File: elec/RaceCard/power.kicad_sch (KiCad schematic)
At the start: 12 parts, among them J1 530480210, Q1 DMP3125L-7, U1 TLV74033PDQNR, U2 MCP73812T-420I_OT, U3 AS11AH

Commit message: Choses manquantes
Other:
- note added: "GÉRER LE POWER OUT"
- note added: "METTRE CONN."
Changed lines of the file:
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@@
+		)
+	)
+	(text "METTRE CONN."
+		(exclude_from_sim no)
+		(at 60.706 85.852 0)
+		(effects
+			(font
+				(size 1.27 1.27)
+				(thickness 0.254)
+				(bold yes)
+				(color 255 0 0 1)
+			)
+		)
+	)
+	(text "GÉRER LE POWER OUT"
+		(exclude_from_sim no)
+		(at 230.124 97.282 0)
+		(effects
+			(font
+				(size 1.27 1.27)
+				(thickness 0.254)
+				(bold yes)
+				(color 255 0 0 1)
+			)
 		)
 	)

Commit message: Commence plugger choses
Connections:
- net VDD: now reaches C2.1, D1.2 (A), U1.1 (OUT)
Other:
- note removed: "GÉRER LE POWER OUT"
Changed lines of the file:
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@@
-		)
-	)
-	(text "GÉRER LE POWER OUT"
-		(exclude_from_sim no)
-		(at 230.124 97.282 0)
-		(effects
-			(font
-				(size 1.27 1.27)
-				(thickness 0.254)
-				(bold yes)
-				(color 255 0 0 1)
-			)
 		)
 	)
@@
 		(color 0 0 0 0)
 	)
+	(junction
+		(at 218.44 97.79)
+		(diameter 0)
+		(color 0 0 0 0)
+	)
 	(wire
 		(pts
@@
 	(wire
 		(pts
+			(xy 218.44 97.79) (xy 222.25 97.79)
+		)
+		(stroke
+			(width 0)
+			(type default)
+		)
+	)
+	(wire
+		(pts
 			(xy 209.55 104.14) (xy 209.55 105.41)
 		)
@@
 	(wire
 		(pts
+			(xy 218.44 97.79) (xy 218.44 99.06)
+		)
+		(stroke
+			(width 0)
+			(type default)
+		)
+	)
+	(wire
+		(pts
 			(xy 191.77 104.14) (xy 190.5 104.14)
 		)
@@
 		(pts
 			(xy 218.44 104.14) (xy 218.44 105.41)
-		)
-		(stroke
-			(width 0)
-			(type default)
-		)
-	)
-	(wire
-		(pts
-			(xy 218.44 97.79) (xy 218.44 99.06)
 		)
 		(stroke
@@
 		)
 	)
+	(hierarchical_label "VDD"
+		(shape output)
+		(at 222.25 97.79 0)
+		(effects
+			(font
+				(size 1.27 1.27)
+			)
+			(justify left)
+		)
+	)

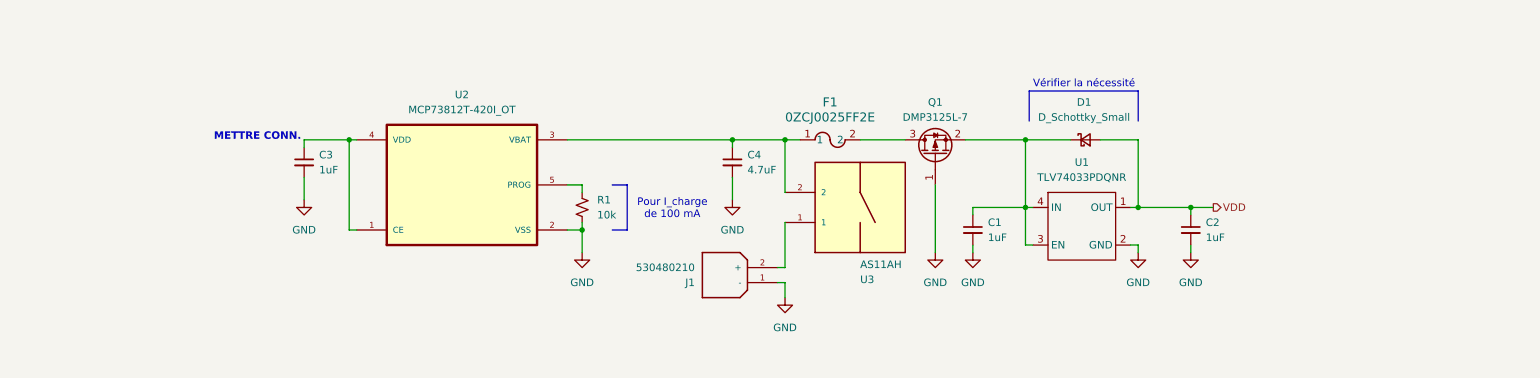
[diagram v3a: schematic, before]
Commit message: ajout connecteur usb c et leds
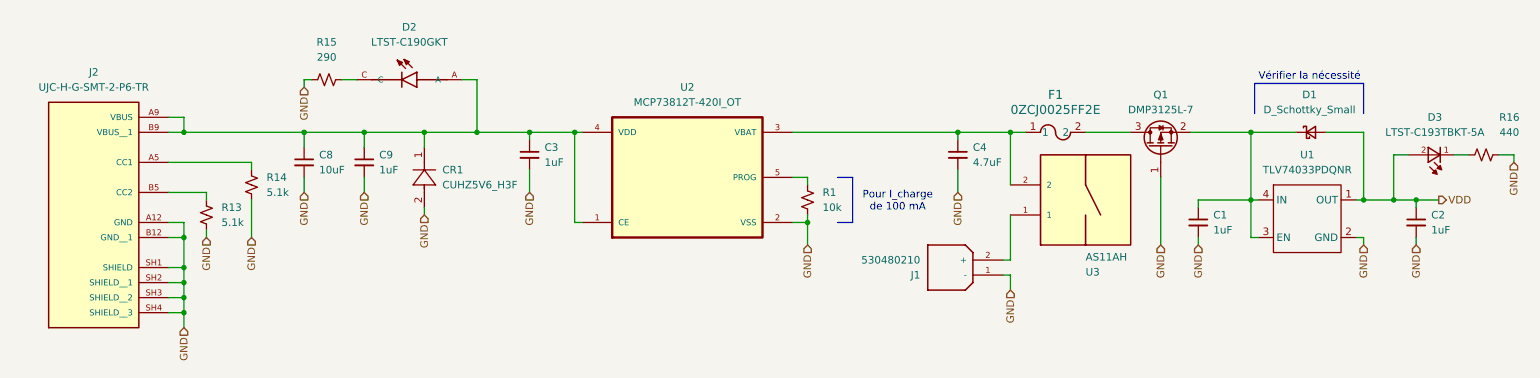
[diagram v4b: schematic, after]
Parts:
- added C8: 10uF, Capacitor_SMD:C_0603_1608Metric, symbol Device:C_Small
- added C9: 1uF, Capacitor_SMD:C_0603_1608Metric, symbol Device:C_Small
- added CR1: CUHZ5V6_H3F, C3I_A25:SOD-323HEUS2H_TOS, symbol C3I_A25:CUHZ5V6_H3F
- added D2: LTST-C190GKT, LTST-C190GKT:LEDM1608X80, symbol C3I_A25:LTST-C190GKT
- added D3: LTST-C193TBKT-5A, LTST-C193TBKT-5A:0603, symbol C3I_A25:LTST-C193TBKT-5A
- added J2: UJC-H-G-SMT-2-P6-TR, UJC-H-G-SMT-2-P6-TR:SAMESKY_UJC-H-G-SMT-2-P6-TR, symbol C3I_A25:UJC-H-G-SMT-2-P6-TR
- added R13, R14: 5.1k, Resistor_SMD:R_0603_1608Metric, symbol Device:R_Small_US
- added R15: 290, Resistor_SMD:R_0603_1608Metric, symbol Device:R_Small_US
- added R16: 440, Resistor_SMD:R_0603_1608Metric, symbol Device:R_Small_US
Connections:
- net GND: now also C8.2, C9.2, CR1.2, J2.A12 (GND), J2.B12 (GND__1), J2.SH1 (SHIELD), J2.SH2 (SHIELD__1), J2.SH3 (SHIELD__2), J2.SH4 (SHIELD__3), R13.2, R14.1, R15.1, R16.2
- net VDD: now also D3.2
- net at C3.1, U2.1 (CE), U2.4 (VDD): now also C8.1, C9.1, CR1.1, D2.A, J2.A9 (VBUS), J2.B9 (VBUS__1)
- new net: D3.1, R16.1
- new net: J2.A5 (CC1), R14.2
- new net: J2.B5 (CC2), R13.1
- new net: D2.C, R15.2
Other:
- note removed: "METTRE CONN."
- moved on the sheet: C1, C2, C3, C4, D1, F1, J1, Q1, R1, U1, U2, U3

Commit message: + test points
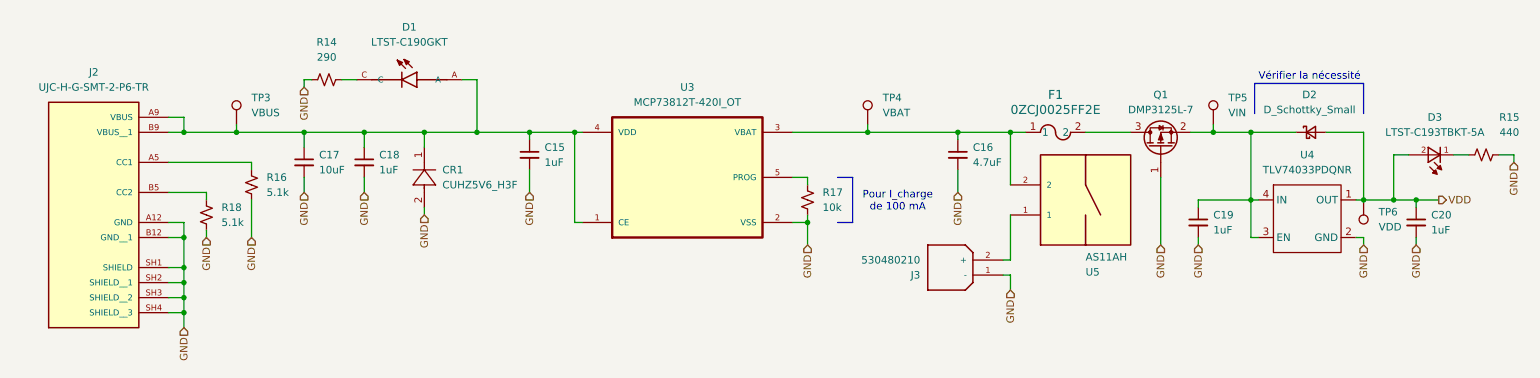
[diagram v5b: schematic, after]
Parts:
- added TP3: VBUS, TestPoint:TestPoint_THTPad_3.0x3.0mm_Drill1.5mm, symbol Connector:TestPoint
- added TP4: VBAT, TestPoint:TestPoint_THTPad_3.0x3.0mm_Drill1.5mm, symbol Connector:TestPoint
- added TP5: VIN, TestPoint:TestPoint_THTPad_3.0x3.0mm_Drill1.5mm, symbol Connector:TestPoint
- added TP6: VDD, TestPoint:TestPoint_THTPad_3.0x3.0mm_Drill1.5mm, symbol Connector:TestPoint
- renumbered C3 to C15, C4 to C16, C8 to C17, C9 to C18, C1 to C19, C2 to C20, D2 to D1, D1 to D2, J1 to J3, R15 to R14, R16 to R15, R14 to R16, R1 to R17, R13 to R18, U2 to U3, U1 to U4, U3 to U5
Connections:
- net VDD: now also TP6.1
- net at C16.1, F1.1, U3.3 (VBAT)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: now also TP4.1
- net at C15.1, C17.1, C18.1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: now also TP3.1
- net at C19.1, D2.1 (K), Q1.2 (S)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: now also TP5.1

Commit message: Fix des footprints et edge cuts
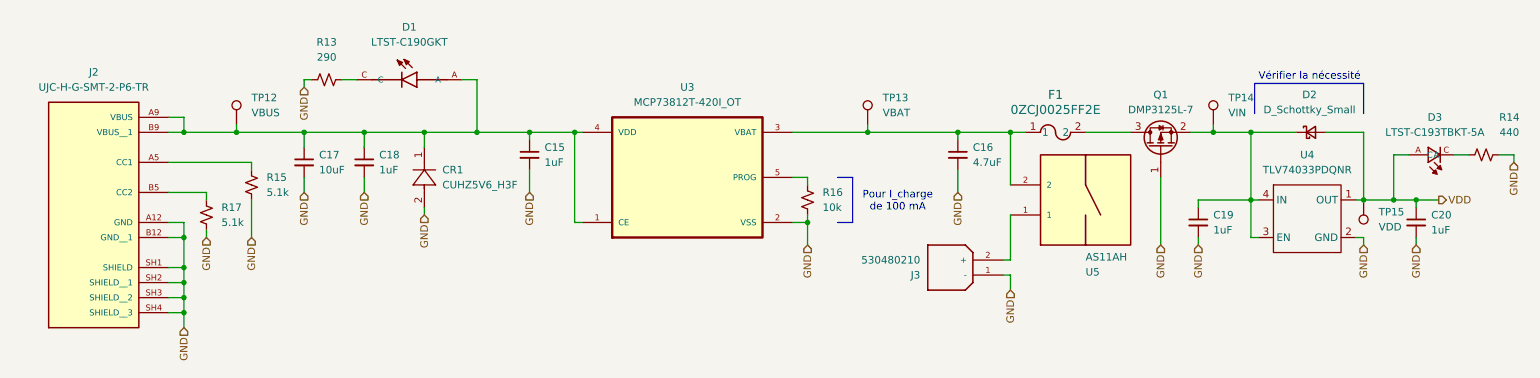
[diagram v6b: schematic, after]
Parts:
- CR1: footprint C3I_A25:SOD-323HEUS2H_TOS -> SOD-323HEUS2H_TOS
- D2: footprint (none) -> Diode_SMD:D_0603_1608Metric
- D3: footprint LTST-C193TBKT-5A:0603 -> C3I_A25:LEDM1608X80
- F1: footprint C3I_A25:0ZCJ_BEL -> 0ZCJ_BEL
- renumbered R14 to R13, R15 to R14, R16 to R15, R17 to R16, R18 to R17, TP3 to TP12, TP4 to TP13, TP5 to TP14, TP6 to TP15
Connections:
- net VDD: now also D3.A; no longer D3.2
- net at R14.1: now also D3.C; no longer D3.1
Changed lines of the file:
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@@
 			)
 		)
-		(property "Footprint" "LTST-C193TBKT-5A:0603"
+		(property "Footprint" "C3I_A25:LEDM1608X80"
 			(at 260.35 88.9 0)
 			(effects
@@
 			)
 		)
-		(pin "2"
-		)
-		(pin "1"
+		(pin "A"
+		)
+		(pin "C"
 		)
 		(instances
@@
 		(dnp no)
 		(fields_autoplaced yes)
-		(property "Reference" "R17"
+		(property "Reference" "R16"
 			(at 156.21 95.2499 0)
 			(effects
@@
 			(project ""
 				(path "/fef6ab1d-cc84-41bb-aff7-8da28fd37bf7/de9963ec-94d0-4cea-b3e4-29f643159c90"
-					(reference "R17")
+					(reference "R16")
 					(unit 1)
 				)
@@
 		(dnp no)
 		(fields_autoplaced yes)
-		(property "Reference" "R16"
+		(property "Reference" "R15"
 			(at 62.23 92.7099 0)
 			(effects
@@
 			(project "RaceCard"
 				(path "/fef6ab1d-cc84-41bb-aff7-8da28fd37bf7/de9963ec-94d0-4cea-b3e4-29f643159c90"
-					(reference "R16")
+					(reference "R15")
 					(unit 1)
 				)
@@
 		(on_board yes)
 		(dnp no)
-		(property "Reference" "R15"
+		(property "Reference" "R14"
 			(at 272.288 82.55 90)
 			(effects
@@
 			(project "RaceCard"
 				(path "/fef6ab1d-cc84-41bb-aff7-8da28fd37bf7/de9963ec-94d0-4cea-b3e4-29f643159c90"
-					(reference "R15")
+					(reference "R14")
+					(unit 1)
+				)
+			)
+		)
+	)
+	(symbol
+		(lib_id "Device:D_Schottky_Small")
+		(at 238.76 85.09 0)
+		(unit 1)
+		(exclude_from_sim no)
+		(in_bom yes)
+		(on_board yes)
+		(dnp no)
+		(fields_autoplaced yes)
+		(property "Reference" "D2"
+			(at 238.506 78.74 0)
+			(effects
+				(font
+					(size 1.27 1.27)
+				)
+			)
+		)
+		(property "Value" "D_Schottky_Small"
+			(at 238.506 81.28 0)
+			(effects
+				(font
+					(size 1.27 1.27)
+				)
+			)
+		)
+		(property "Footprint" "Diode_SMD:D_0603_1608Metric"
+			(at 238.76 85.09 90)
+			(effects
+				(font
+					(size 1.27 1.27)
+				)
+				(hide yes)
+			)
+		)
+		(property "Datasheet" "~"
+			(at 238.76 85.09 90)
+			(effects
+				(font
+					(size 1.27 1.27)
+				)
+				(hide yes)
+			)
+		)
+		(property "Description" "Schottky diode, small symbol"
+			(at 238.76 85.09 0)
+			(effects
+				(font
+					(size 1.27 1.27)
+				)
+				(hide yes)
+			)
+		)
+		(pin "1"
+		)
+		(pin "2"
+		)
+		(instances
+			(project ""
+				(path "/fef6ab1d-cc84-41bb-aff7-8da28fd37bf7/de9963ec-94d0-4cea-b3e4-29f643159c90"
+					(reference "D2")
 					(unit 1)
 				)
@@
 			)
 		)
-		(property "Footprint" "C3I_A25:0ZCJ_BEL"
+		(property "Footprint" "0ZCJ_BEL"
 			(at 190.5 85.09 0)
 			(effects
@@
 		(dnp no)
 		(fields_autoplaced yes)
-		(property "Reference" "TP3"
+		(property "Reference" "TP12"
 			(at 59.69 79.2479 0)
 			(effects
@@
 			(project "RaceCard"
 				(path "/fef6ab1d-cc84-41bb-aff7-8da28fd37bf7/de9963ec-94d0-4cea-b3e4-29f643159c90"
-					(reference "TP3")
+					(reference "TP12")
 					(unit 1)
 				)
@@
 		(dnp no)
 		(fields_autoplaced yes)
-		(property "Reference" "TP5"
+		(property "Reference" "TP14"
 			(at 224.79 79.2479 0)
 			(effects
@@
 			(project "RaceCard"
 				(path "/fef6ab1d-cc84-41bb-aff7-8da28fd37bf7/de9963ec-94d0-4cea-b3e4-29f643159c90"
-					(reference "TP5")
+					(reference "TP14")
 					(unit 1)
 				)
@@
 			)
 		)
-		(property "Footprint" "C3I_A25:SOD-323HEUS2H_TOS"
+		(property "Footprint" "SOD-323HEUS2H_TOS"
 			(at 88.9 97.79 0)
 			(effects
@@
 		(dnp no)
 		(fields_autoplaced yes)
-		(property "Reference" "R18"
+		(property "Reference" "R17"
 			(at 54.61 97.7899 0)
 			(effects
@@
 			(project "RaceCard"
 				(path "/fef6ab1d-cc84-41bb-aff7-8da28fd37bf7/de9963ec-94d0-4cea-b3e4-29f643159c90"
-					(reference "R18")
+					(reference "R17")
 					(unit 1)
 				)
@@
 		(dnp no)
 		(fields_autoplaced yes)
-		(property "Reference" "R14"
+		(property "Reference" "R13"
 			(at 72.39 69.85 90)
 			(effects
@@
 			(project "RaceCard"
 				(path "/fef6ab1d-cc84-41bb-aff7-8da28fd37bf7/de9963ec-94d0-4cea-b3e4-29f643159c90"
-					(reference "R14")
+					(reference "R13")
 					(unit 1)
 				)
@@
 		(dnp no)
 		(fields_autoplaced yes)
-		(property "Reference" "TP4"
+		(property "Reference" "TP13"
 			(at 166.37 79.2479 0)
 			(effects
@@
 			(project "RaceCard"
 				(path "/fef6ab1d-cc84-41bb-aff7-8da28fd37bf7/de9963ec-94d0-4cea-b3e4-29f643159c90"
-					(reference "TP4")
+					(reference "TP13")
 					(unit 1)
 				)
@@
 	)
 	(symbol
-		(lib_id "Device:D_Schottky_Small")
-		(at 238.76 85.09 0)
-		(unit 1)
-		(exclude_from_sim no)
-		(in_bom yes)
-		(on_board yes)
-		(dnp no)
-		(fields_autoplaced yes)
-		(property "Reference" "D2"
-			(at 238.506 78.74 0)
-			(effects
-				(font
-					(size 1.27 1.27)
-				)
-			)
-		)
-		(property "Value" "D_Schottky_Small"
-			(at 238.506 81.28 0)
-			(effects
-				(font
-					(size 1.27 1.27)
-				)
-			)
-		)
-		(property "Footprint" ""
-			(at 238.76 85.09 90)
-			(effects
-				(font
-					(size 1.27 1.27)
-				)
-				(hide yes)
-			)
-		)
-		(property "Datasheet" "~"
-			(at 238.76 85.09 90)
-			(effects
-				(font
-					(size 1.27 1.27)
-				)
-				(hide yes)
-			)
-		)
-		(property "Description" "Schottky diode, small symbol"
-			(at 238.76 85.09 0)
-			(effects
-				(font
-					(size 1.27 1.27)
-				)
-				(hide yes)
-			)
-		)
-		(pin "2"
-		)
-		(pin "1"
-		)
-		(instances
-			(project ""
-				(path "/fef6ab1d-cc84-41bb-aff7-8da28fd37bf7/de9963ec-94d0-4cea-b3e4-29f643159c90"
-					(reference "D2")
-					(unit 1)
-				)
-			)
-		)
-	)
-	(symbol
 		(lib_id "Connector:TestPoint")
 		(at 247.65 96.52 180)
@@
 		(dnp no)
 		(fields_autoplaced yes)
-		(property "Reference" "TP6"
+		(property "Reference" "TP15"
 			(at 250.19 98.5519 0)
 			(effects
@@
 			(project "RaceCard"
 				(path "/fef6ab1d-cc84-41bb-aff7-8da28fd37bf7/de9963ec-94d0-4cea-b3e4-29f643159c90"
-					(reference "TP6")
-					(unit 1)
-				)
+					(reference "TP15")
+					(unit 1)
+				)

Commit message: Tout le power est routed
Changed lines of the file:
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@@
 		(on_board yes)
 		(dnp no)
-		(fields_autoplaced yes)
 		(property "Reference" "TP14"
-			(at 224.79 79.2479 0)
+			(at 223.774 79.248 0)
 			(effects
 				(font
@@
 		)
 		(property "Value" "VIN"
-			(at 224.79 81.7879 0)
+			(at 223.774 81.788 0)
 			(effects
 				(font

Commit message: Power net update et cleanup sch
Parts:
- R12: renamed from R13; value 290 -> 290R
- R13: renamed from R14; value 440 -> 440R
- renumbered C16 to C17, C17 to C18, C18 to C19, C15 to C20, C19 to C21, C20 to C22, R16 to R14, R17 to R16, TP12 to TP13, TP13 to TP14, TP14 to TP15, TP15 to TP16
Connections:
- net GND: now also D1.C; no longer R12.1
- net at C18.1, C19.1, C20.1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: now also R12.1; no longer D1.A
- net at R12.2: now also D1.A; no longer D1.C
- net VDD renamed +3V3
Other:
- moved on the sheet: C18, C19, C20, C21, C22, CR1, D1, D3, R12, R13, R15, R16
